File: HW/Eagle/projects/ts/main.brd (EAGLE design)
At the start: 80 x 45 mm, 46 parts, among them IC1 4050D, T1 IRFZ24N, T2 IRFZ24N, U1 ATMEGA328P-PU, U2 LM2576T, U3 HT7533, U4 LM75

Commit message: HW Release 1
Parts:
- LED1: device led:LED3MM -> led:LED5MM
- moved R10 18.8 mm to (38.0, 5.00), turned to 90 degrees
- moved R9 3.54 mm to (47.5, 3.00)
- moved C11 2.55 mm to (29.0, 30.0)
- moved IC1 2.55 mm to (35.5, 32.0)
- moved LED1 1.41 mm to (42.5, 5.00)
- moved R4 1.12 mm to (43.5, 35.5)
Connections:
- removed net N$2: R4.1
- net LCD_LED_5V: now also R4.1, U1.16; no longer U1.5
- net LED: now also U1.15; no longer U1.16
- net OUT2: now also U1.5; no longer U1.15
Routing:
- net LCD_LED_5V: track 0.00 -> 51.1 mm, vias 0 -> 3
- net VCC: track 221.7 -> 208.9 mm
- net OUT2: track 13.0 -> 24.8 mm, vias 0 -> 1
- net +3V3: track 33.3 -> 29.3 mm
- net LCD_SCE_5V: track 43.3 -> 47.0 mm
- net N$9: track 34.6 -> 31.1 mm
- net LCD_DC_5V: track 34.4 -> 37.4 mm
- net SCK: track 59.2 -> 62.2 mm
- net LED: track 24.9 -> 22.4 mm
- net N$6: track 3.84 -> 6.15 mm
- net LCD_SCK: track 4.06 -> 5.62 mm
- net LCD_RST: track 13.9 -> 15.5 mm
- net LCD_DC: track 4.32 -> 5.85 mm
- net NRST: track 90.5 -> 91.8 mm
- net LCD_MOSI: track 4.06 -> 5.33 mm
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
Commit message: Minor HW changes
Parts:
- added H1: MOUNT-PAD-ROUND3.6, holes:3,6-PAD
- moved LED1 0.25 mm to (42.8, 5.00)
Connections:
- net GND: now also H1.B3,6
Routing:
- net +12V: track 29.8 -> 32.6 mm
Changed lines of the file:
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@@
 <attribute name="MF" value="" x="47.5" y="26.5" size="1.778" layer="27" display="off"/>
 <attribute name="OC_FARNELL" value="unknown" x="47.5" y="26.5" size="1.778" layer="27" display="off"/>
-<attribute name="NAME" x="45.69" y="29.171" size="1.27" layer="25" ratio="10"/>
+<attribute name="NAME" x="45.69" y="29.671" size="1.27" layer="25" ratio="10"/>
 <attribute name="VALUE" x="46.23" y="22.309" size="1.27" layer="27" ratio="10"/>
 </element>
@@
 <element name="D1" library="misc" package="DIODE5MM" value="1N582X" x="22" y="10.5" smashed="yes" rot="R270">
 <attribute name="VALUE" x="19.841" y="13.04" size="1.27" layer="27" ratio="10" rot="R270"/>
-<attribute name="NAME" x="23.92" y="3.421" size="1.27" layer="25" ratio="10"/>
+<attribute name="NAME" x="23.92" y="3.921" size="1.27" layer="25" ratio="10"/>
 </element>
 <element name="C6" library="rcl" package="TAP5-80" value="100uF" x="14.5" y="6" smashed="yes" rot="R270">
@@
 </element>
 <element name="C7" library="rcl" package="TT5D10" value="1000uF" x="14" y="26.5" smashed="yes">
-<attribute name="NAME" x="18.691" y="29.802" size="1.27" layer="25" ratio="10"/>
+<attribute name="NAME" x="17.191" y="30.802" size="1.27" layer="25" ratio="10"/>
 <attribute name="VALUE" x="10.698" y="23.452" size="1.27" layer="27" ratio="10"/>
 </element>
@@
 <attribute name="MF" value="" x="50.5" y="36" size="1.778" layer="27" rot="R270" display="off"/>
 <attribute name="OC_FARNELL" value="unknown" x="50.5" y="36" size="1.778" layer="27" rot="R270" display="off"/>
-<attribute name="NAME" x="52.81" y="32.099" size="1.27" layer="25" ratio="10" rot="R180"/>
+<attribute name="NAME" x="48.599" y="33.94" size="1.27" layer="25" ratio="10" rot="R90"/>
 <attribute name="VALUE" x="47.579" y="39.81" size="1.27" layer="27" ratio="10" rot="R270"/>
 </element>
@@
 </element>
 <element name="T1" library="misc" package="TO220AB" value="IRFZ24N" x="30" y="21" smashed="yes" rot="R90">
-<attribute name="NAME" x="26.92" y="26.9948" size="1.27" layer="25" ratio="10"/>
+<attribute name="NAME" x="31.92" y="25.9948" size="1.27" layer="25" ratio="10"/>
 <attribute name="VALUE" x="35.08" y="15.92" size="1.27" layer="27" ratio="10" rot="R90"/>
 </element>
 <element name="T2" library="misc" package="TO220AB" value="IRFZ24N" x="36.5" y="21" smashed="yes" rot="R90">
-<attribute name="NAME" x="39" y="24.5" size="1.27" layer="25" ratio="10"/>
+<attribute name="NAME" x="38.5" y="26" size="1.27" layer="25" ratio="10"/>
 <attribute name="VALUE" x="41.58" y="15.92" size="1.27" layer="27" ratio="10" rot="R90"/>
 </element>
@@
 </element>
 <element name="D2" library="diode" package="SMB" value="SS210" x="30.5" y="12.5" smashed="yes">
-<attribute name="NAME" x="26.341" y="10.341" size="1.27" layer="25" rot="R90"/>
+<attribute name="NAME" x="26.341" y="11.841" size="1.27" layer="25" rot="R90"/>
 <attribute name="VALUE" x="28.341" y="9.071" size="1.27" layer="27"/>
 </element>
@@
 <attribute name="VALUE" x="50.365" y="4.46" size="1.27" layer="27"/>
 </element>
-<element name="LED1" library="led" package="LED5MM" value="" x="42.5" y="5" smashed="yes">
-<attribute name="NAME" x="45.175" y="4.5334" size="1.27" layer="25" ratio="10"/>
-<attribute name="VALUE" x="45.7004" y="3.1966" size="1.27" layer="27" ratio="10"/>
-</element>
+<element name="LED1" library="led" package="LED5MM" value="" x="42.75" y="5" smashed="yes">
+<attribute name="NAME" x="45.425" y="4.5334" size="1.27" layer="25" ratio="10"/>
+<attribute name="VALUE" x="45.9504" y="3.1966" size="1.27" layer="27" ratio="10"/>
+</element>
+<element name="H1" library="holes" package="3,6-PAD" value="MOUNT-PAD-ROUND3.6" x="23.5" y="28.5"/>
 </elements>
 <signals>
@@
 <vertex x="21.5" y="21" curve="90"/>
 <vertex x="18.5" y="24"/>
-<vertex x="17.5" y="24"/>
-<vertex x="12.5" y="29"/>
+<vertex x="17" y="24"/>
+<vertex x="12" y="29"/>
 <vertex x="0" y="29"/>
 </polygon>
@@
 <via x="60" y="43.5" extent="1-16" drill="0.5"/>
 <via x="63.5" y="40.5" extent="1-16" drill="0.5"/>
-<via x="22" y="14" extent="1-16" drill="0.5"/>
+<via x="21" y="11.5" extent="1-16" drill="0.5"/>
 <contactref element="C1" pad="2"/>
 <via x="58.85" y="20.5" extent="1-16" drill="0.5"/>
@@
 <contactref element="T1" pad="S"/>
 <via x="41.5" y="35.5" extent="1-16" drill="0.5"/>
-<via x="18.5" y="10.5" extent="1-16" drill="0.5"/>
+<via x="18.5" y="10" extent="1-16" drill="0.5"/>
 <via x="59.25" y="37.75" extent="1-16" drill="0.5"/>
 <via x="58" y="5" extent="1-16" drill="0.5"/>
@@
 <via x="38.5" y="31" extent="1-16" drill="0.5"/>
 <via x="36" y="33" extent="1-16" drill="0.5"/>
+<contactref element="H1" pad="B3,6"/>
+<via x="25.5" y="11.25" extent="1-16" drill="0.5"/>
+<via x="25.5" y="8.75" extent="1-16" drill="0.5"/>
 </signal>
 <signal name="VCC">
@@
 <wire x1="40" y1="10" x2="30" y2="10" width="0.7" layer="16"/>
 <via x="30" y="10" extent="1-16" drill="0.5"/>
-<wire x1="14.46" y1="12.6" x2="28.2" y2="12.6" width="0.7" layer="1"/>
 <wire x1="28.2" y1="12.6" x2="28.3" y2="12.5" width="0.7" layer="1"/>
 <wire x1="28.3" y1="12.5" x2="28.3" y2="11.7" width="0.7" layer="1"/>
@@
 <wire x1="40" y1="10" x2="40.45" y2="10.45" width="0.7" layer="1"/>
 <wire x1="40.45" y1="10.45" x2="40.45" y2="12.5" width="0.7" layer="1"/>
+<wire x1="14.46" y1="12.6" x2="17.9" y2="12.6" width="0.7" layer="16"/>
+<wire x1="17.9" y1="12.6" x2="20.5" y2="10" width="0.7" layer="16"/>
+<wire x1="20.5" y1="10" x2="30" y2="10" width="0.7" layer="16"/>
 </signal>
 <signal name="N$8">
@@
 <wire x1="52.5" y1="9" x2="51.95" y2="9" width="0.25" layer="1"/>
 <contactref element="U1" pad="5"/>
-<wire x1="58" y1="16" x2="56.25" y2="14.25" width="0.25" layer="16"/>
-<wire x1="56.25" y1="14.25" x2="54" y2="14.25" width="0.25" layer="16"/>
+<wire x1="58" y1="15.5" x2="56.75" y2="14.25" width="0.25" layer="16"/>
+<wire x1="56.75" y1="14.25" x2="54" y2="14.25" width="0.25" layer="16"/>
 <wire x1="54" y1="14.25" x2="52.25" y2="12.5" width="0.25" layer="16"/>
 <wire x1="52.25" y1="12.5" x2="52.25" y2="11" width="0.25" layer="16"/>
@@
 <wire x1="52.25" y1="11" x2="52.25" y2="9" width="0.25" layer="1"/>
 <wire x1="52.25" y1="9" x2="51.95" y2="9" width="0.25" layer="1"/>
-<wire x1="58" y1="16" x2="58" y2="26.24" width="0.25" layer="16"/>
+<wire x1="58" y1="15.5" x2="58" y2="26.24" width="0.25" layer="16"/>
 <wire x1="58" y1="26.24" x2="55.88" y2="28.36" width="0.25" layer="16"/>
 </signal>
@@
 <contactref element="LED1" pad="K"/>
 <contactref element="U1" pad="15"/>
-<wire x1="43.77" y1="5" x2="49" y2="5" width="0.25" layer="16"/>
+<wire x1="44.02" y1="5" x2="49" y2="5" width="0.25" layer="16"/>
 <wire x1="49" y1="5" x2="52" y2="2" width="0.25" layer="16"/>
 <wire x1="52" y1="2" x2="60" y2="2" width="0.25" layer="16"/>
@@
 <contactref element="R9" pad="2"/>
 <contactref element="LED1" pad="A"/>
-<wire x1="46.55" y1="3" x2="43.23" y2="3" width="0.25" layer="1"/>
-<wire x1="43.23" y1="3" x2="41.23" y2="5" width="0.25" layer="1"/>
+<wire x1="46.55" y1="3" x2="43.48" y2="3" width="0.25" layer="1"/>
+<wire x1="43.48" y1="3" x2="41.48" y2="5" width="0.25" layer="1"/>
 </signal>
 <signal name="N$10">

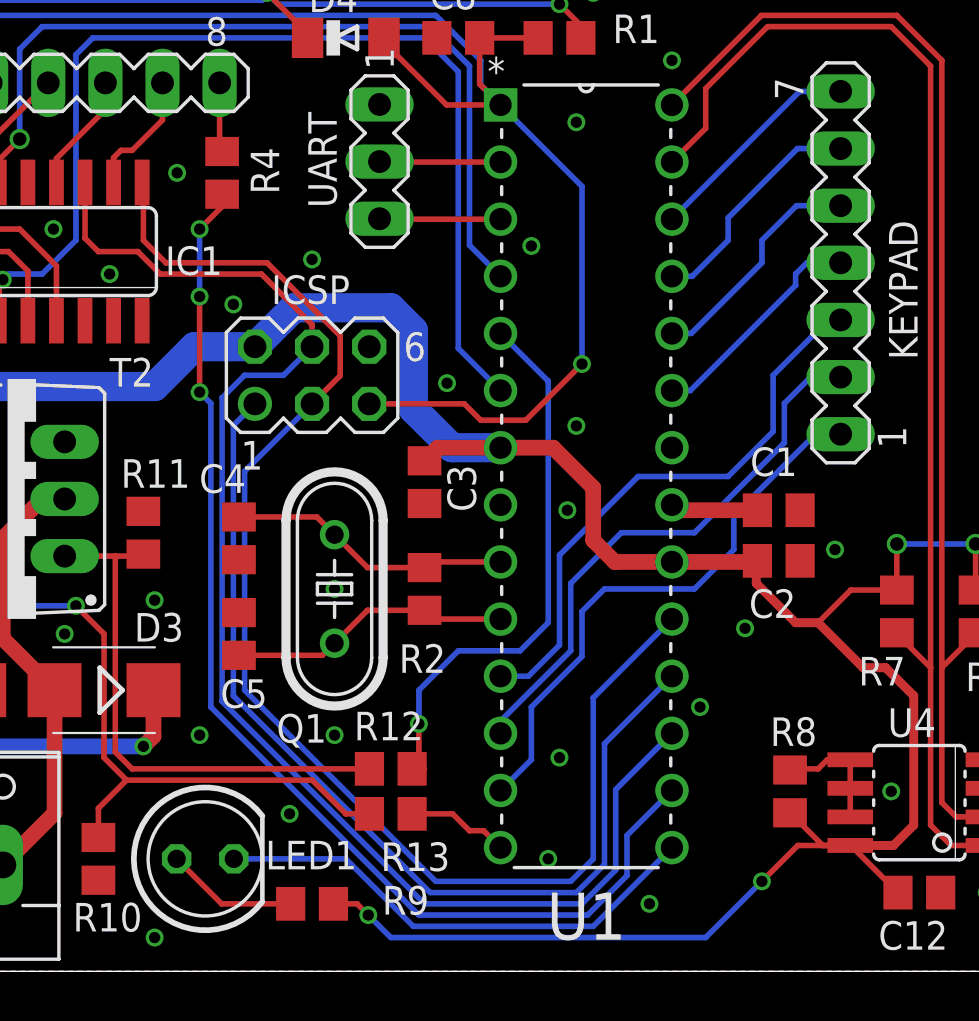
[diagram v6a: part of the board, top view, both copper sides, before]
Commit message: Timer 1 is no longer used for PWM
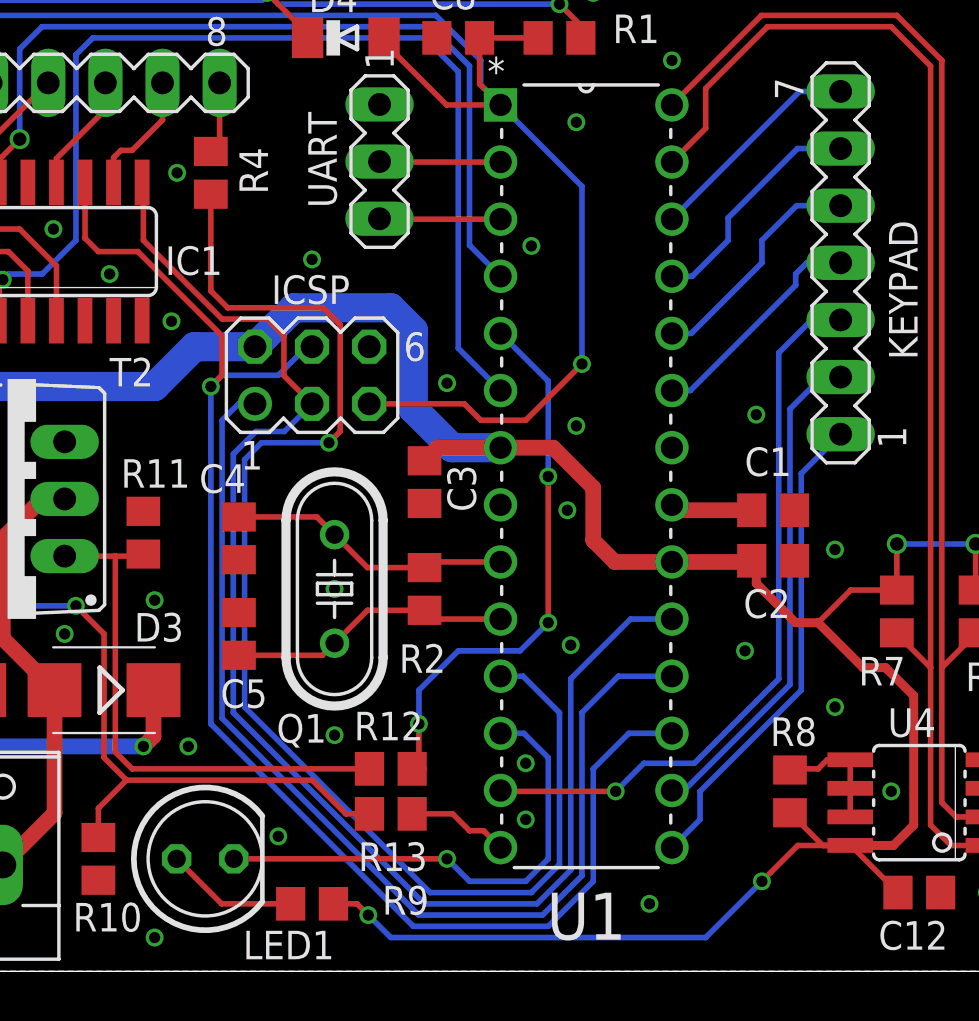
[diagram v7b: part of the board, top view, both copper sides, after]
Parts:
- moved R4 0.50 mm to (43.0, 35.5)
- moved C1 0.25 mm to (68.0, 20.5)
- moved C2 0.25 mm to (68.0, 18.2)
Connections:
- net KEYPAD_C0: now also U1.15; no longer U1.13
- net KEYPAD_C1: now also U1.16; no longer U1.12
- net KEYPAD_C2: now also U1.13; no longer U1.11
- net LCD_LED_5V: now also U1.11; no longer U1.16
- net LED: now also U1.12; no longer U1.15
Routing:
- net LCD_LED_5V: track 51.1 -> 59.2 mm, vias 3 -> 1
- net KEYPAD_C2: track 25.5 -> 32.3 mm, vias 0 -> 1
- net MISO: track 43.6 -> 47.3 mm
- net KEYPAD_C0: track 25.1 -> 21.5 mm
- net KEYPAD_C1: track 24.8 -> 22.3 mm
- net MOSI: track 63.3 -> 64.5 mm, vias 0 -> 1
- net SCK: track 62.2 -> 63.3 mm
- net LED: track 22.2 -> 21.9 mm, vias 0 -> 1
- net OUT2: vias 1 -> 3

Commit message: Minor HW Updates
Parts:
- moved C4 0.50 mm to (44.8, 19.2)
- moved C5 0.50 mm to (44.8, 15.0)
- moved R9 0.50 mm to (47.0, 3.00), turned to 90 degrees
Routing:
- net LED: track 21.9 -> 12.4 mm
- net N$6: track 5.90 -> 0.00 mm
- net VCC: track 209.2 -> 206.0 mm, vias 8 -> 7
- net SCK: track 63.3 -> 65.9 mm
- net LCD_LED_5V: track 59.2 -> 61.1 mm
- net MISO: track 47.3 -> 49.1 mm
- net MOSI: track 64.5 -> 65.9 mm
- net N$4: track 12.7 -> 12.2 mm
- net N$3: track 12.6 -> 12.1 mm
